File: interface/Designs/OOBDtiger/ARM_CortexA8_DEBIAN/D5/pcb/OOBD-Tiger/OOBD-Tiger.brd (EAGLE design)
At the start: 63.4 x 38.2 mm, 112 parts, among them IC1 ADM3053M, IC2 ADM3053M, IC4 DS3231, U1 SY6280, U10 MP1482DS, U2 SN65HVD230(SO8), U3 SY6280, U6 SN65HVD230(SO8)

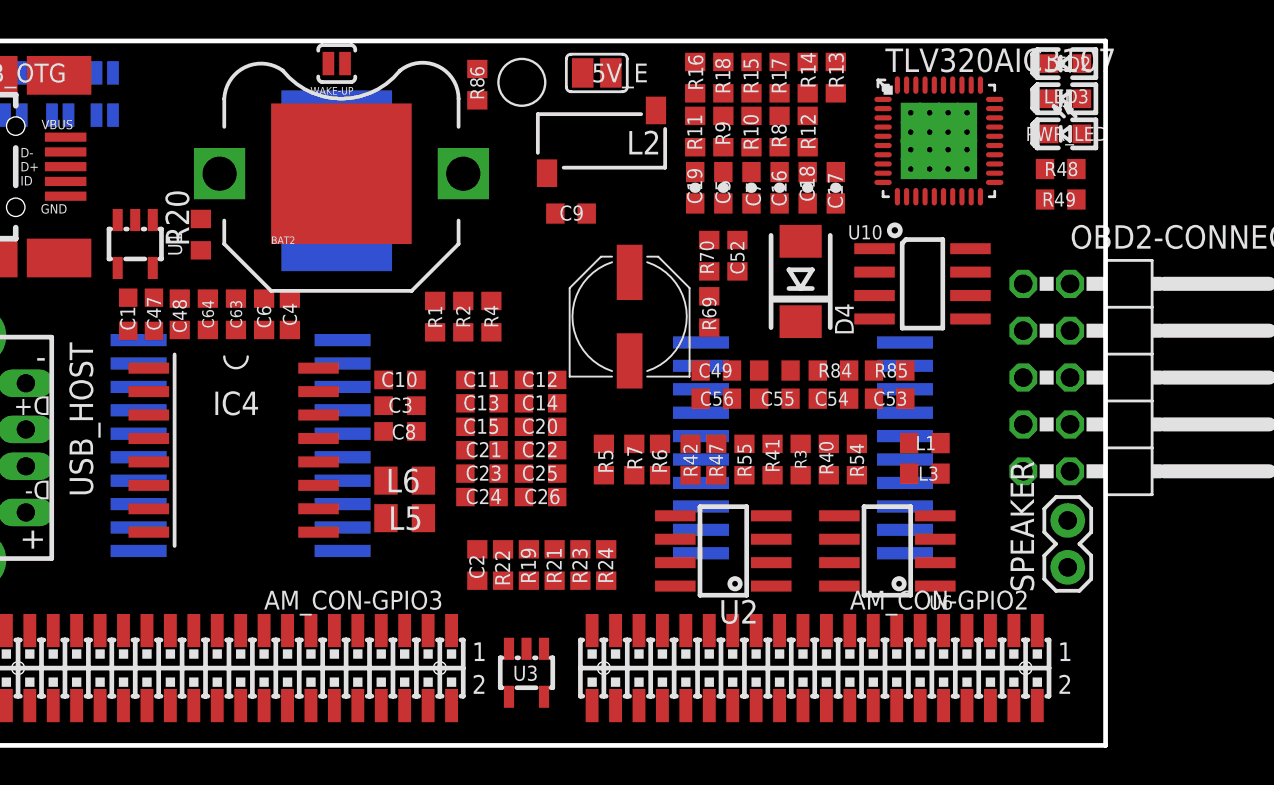
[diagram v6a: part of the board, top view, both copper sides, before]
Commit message: Erster adm3053 Plazierungsversuch, Kondensatoren nahe an IC, aber nicht so nah wie in der Alpnote.
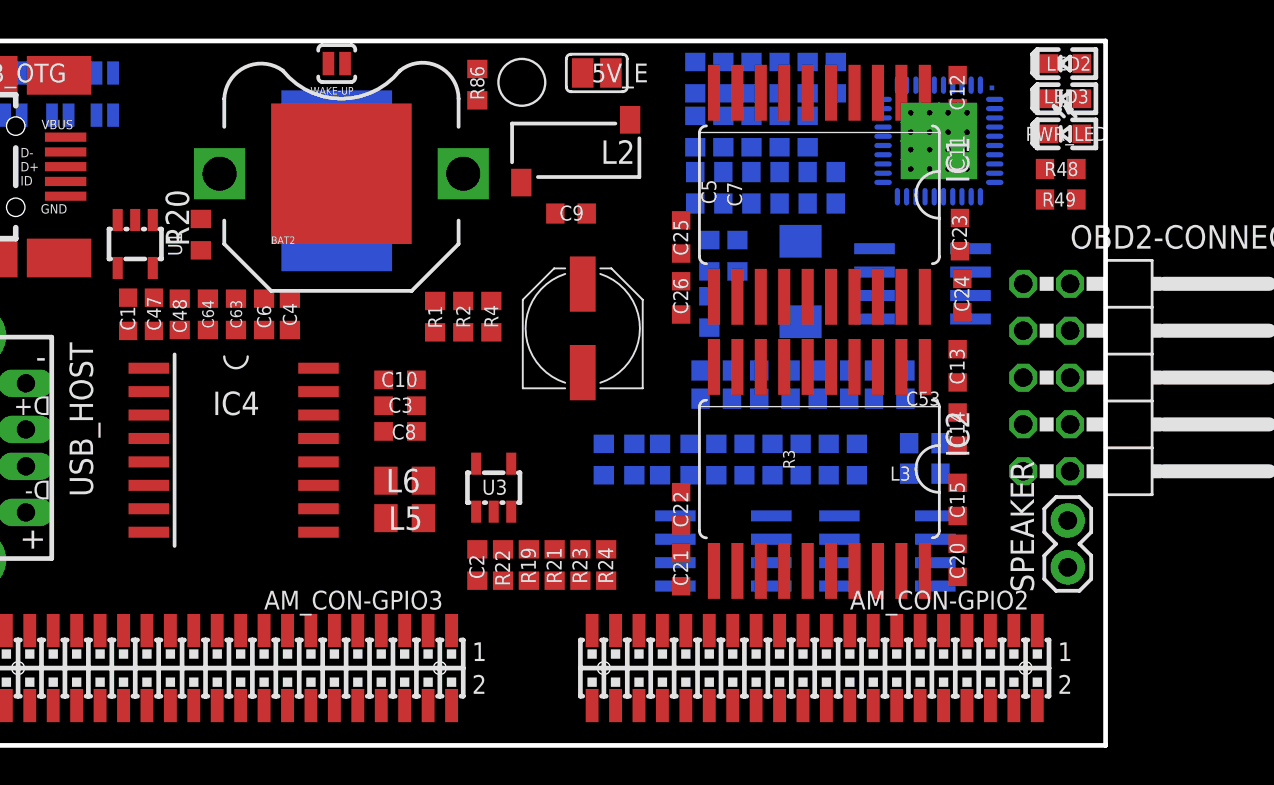
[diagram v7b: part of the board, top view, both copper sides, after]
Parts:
- moved IC1 34.2 mm to (47.9, 29.8), flipped to the top, turned to 180 degrees
- moved C23 29.0 mm to (55.5, 27.7), turned to 90 degrees
- moved C11 28.6 mm to (55.4, 32.1), turned to 90 degrees
- moved C24 28.2 mm to (55.6, 24.4), turned to 90 degrees
- moved C12 27.5 mm to (55.4, 35.4), turned to 90 degrees
- moved C15 26.1 mm to (55.4, 13.3), turned to 90 degrees
- moved C13 25.9 mm to (55.4, 20.6), turned to 90 degrees
- moved C20 23.7 mm to (55.4, 10.0), turned to 90 degrees
- moved C14 22.6 mm to (55.4, 17.1), turned to 90 degrees
- moved C25 14.9 mm to (40.4, 27.6), turned to 90 degrees
- moved C26 13.2 mm to (40.4, 24.3), turned to 90 degrees
- moved C21 12.6 mm to (40.4, 9.53), turned to 90 degrees
- moved U3 10.2 mm to (30.2, 14.0), turned to 270 degrees
- moved C22 8.26 mm to (40.4, 12.8), turned to 90 degrees
- moved C51 2.62 mm to (35.1, 22.6)
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
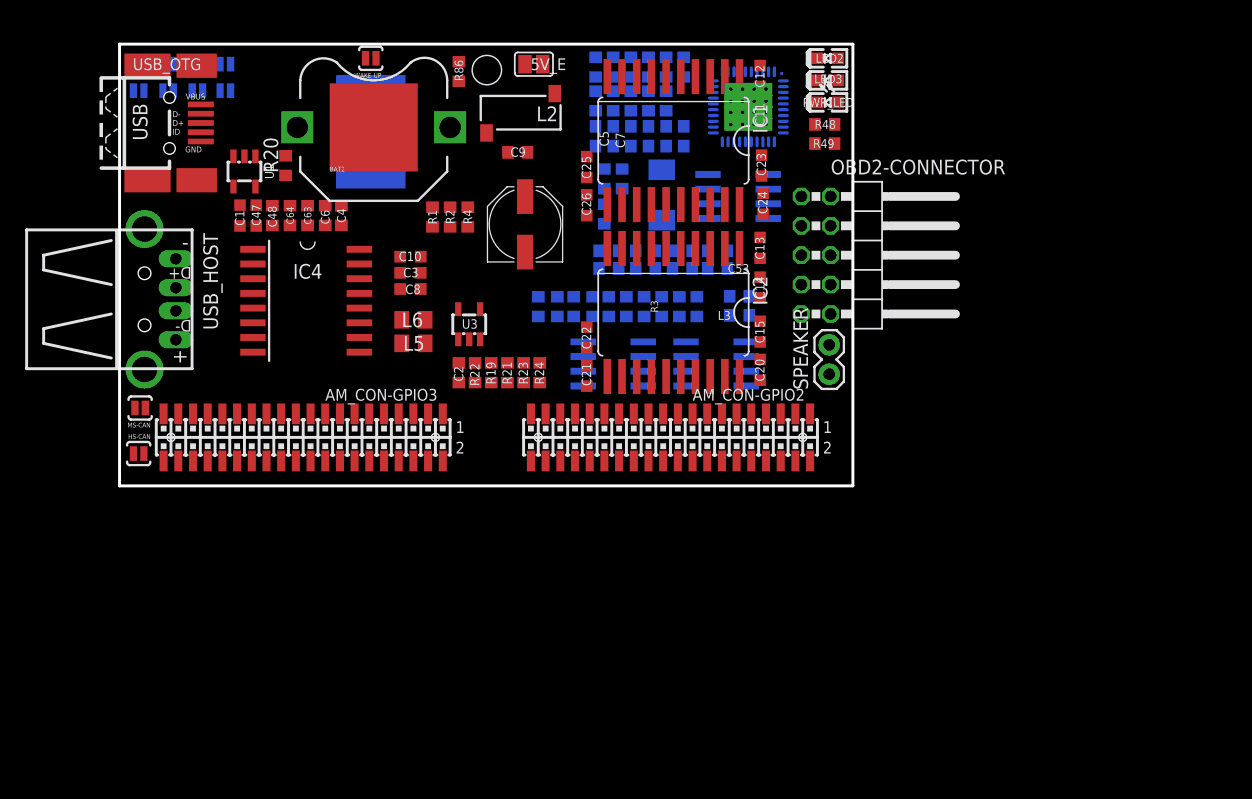
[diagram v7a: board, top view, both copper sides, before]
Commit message: fix ERC findings modify and fix ADM3053 connections remove jumper against optional 0R resistors for Standard CAN interface
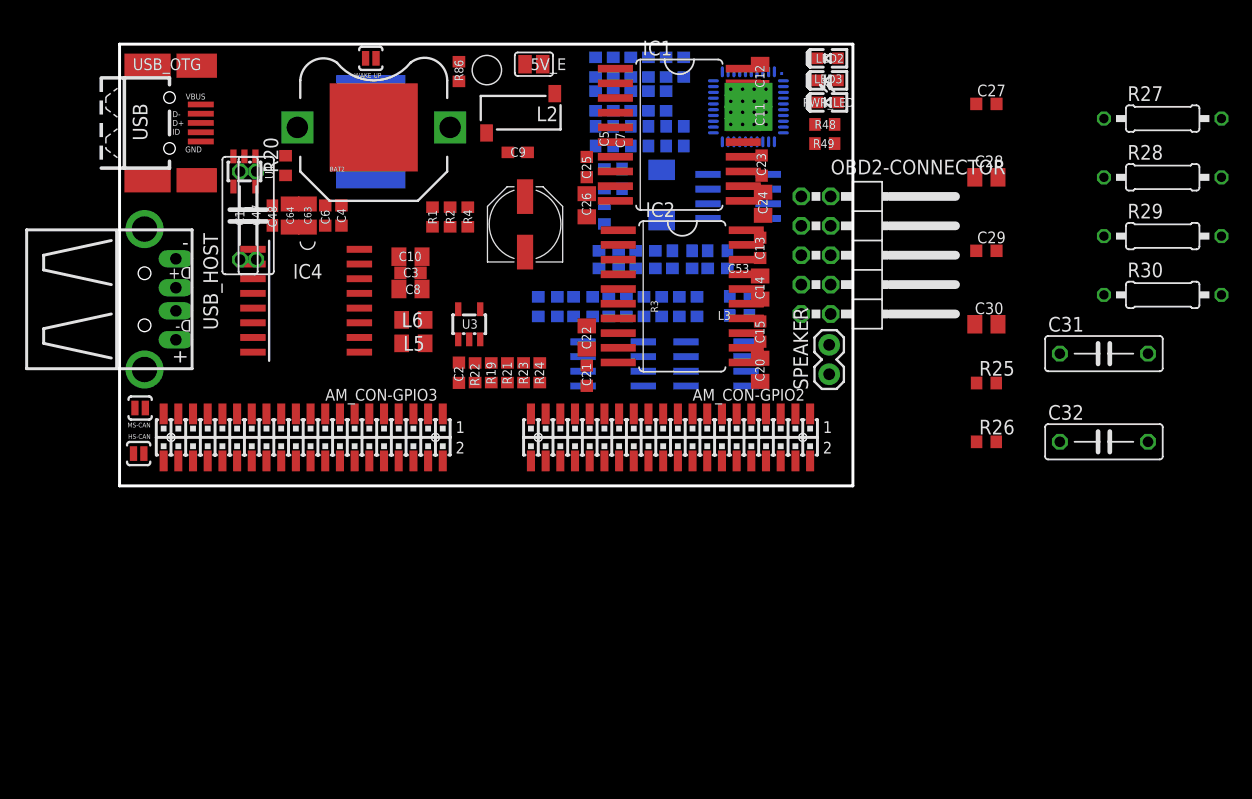
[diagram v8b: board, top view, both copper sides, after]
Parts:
- removed HS-CAN_H-DISABLE, HS-CAN_L-DISABLE, MS-CAN_H-DISABLE, MS-CAN_L-DISABLE: CLOSED, SparkFun:SJ_2S-NO
- removed HS-CAN_H-ENABLE, HS-CAN_L-ENABLE, MS-CAN_H-ENABLE, MS-CAN_L-ENABLE: OPEN (use jumper), SparkFun:SJ_2S-NO
- added C27, C29: 100nF, rcl:C0603K
- added C28, C30: 10µF, rcl:C0805K
- added C31, C32: NA (AY2221K29Y5SS63L7), rcl:C075-032X103
- added R25, R26: 8k2, rcl:R0603
- added R27, R28, R29, R30: NA (0R), rcl:0207/10
- C1, C47: device rcl:C0603_OLIMEX -> rcl:C075-032X103
- C10, C8: device rcl:C0603_DWS -> rcl:C0805K
- C11, C13, C15, C21, C23, C25: device rcl:C0603_OLIMEX -> rcl:C0603K
- C12, C14, C20, C22, C24, C26: device rcl:C0603_OLIMEX -> rcl:C0805K
- C2, C4, C6: device rcl:C0603 -> rcl:C0603K
- C3: device rcl:C0603_DWS -> rcl:C0603K
- C63, C64: device rcl:C0603 -> rcl:C0805K
- moved IC2 1.59 mm to (48.6, 16.4), turned to 270 degrees
- moved IC1 0.72 mm to (48.4, 30.4), turned to 270 degrees
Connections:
- removed net CANH: IC2.17, MS-CAN_H-ENABLE.1
- removed net CANH1: HS-CAN_H-ENABLE.2, HS-CAN_L-DISABLE.1, OBD2-CONNECTOR.7
- removed net CANL: MS-CAN.1, MS-CAN_L-DISABLE.2, U6.6
- removed net CANL1: HS-CAN.1, HS-CAN_H-DISABLE.1, U2.6
- removed net GND1: IC1.9
- removed net N$30: HS-CAN_L-DISABLE.2, R6.2, U2.7
- removed net N$32: IC2.15, MS-CAN_L-ENABLE.2
- removed net N$36: MS-CAN_L-DISABLE.1, MS-CAN_L-ENABLE.1, OBD2-CONNECTOR.2
- removed net N$37: MS-CAN_H-DISABLE.1, MS-CAN_H-ENABLE.2, OBD2-CONNECTOR.1
- removed net N$38: IC2.11, IC2.13, IC2.14, IC2.16
- removed net N$40: IC1.19
- removed net N$42: IC2.10, IC2.20, IC2.9
- removed net N$45: IC1.11, IC1.13, IC1.14, IC1.16
- removed net N$46: IC1.10, IC1.20
- removed net VCC: AM3352-SOM-EVB-PLATFORM.3-3, AM3352-SOM-EVB-PLATFORM.4-3, C1.1, C47.1, R47.2, U2.3, U6.3
- new net 3V3: AM3352-SOM-EVB-PLATFORM.3-3, AM3352-SOM-EVB-PLATFORM.4-3, C1.1, C11.1, C12.1, C13.1, C14.1, C47.1, IC1.8, IC2.8, R47.2, U2.3, U6.3
- new net CAN0_H: IC2.17, OBD2-CONNECTOR.1, R42.2, U6.7
- new net CAN0_L: IC2.15, MS-CAN.1, OBD2-CONNECTOR.2, U6.6
- new net CAN1_H: IC1.17, OBD2-CONNECTOR.7, R6.2, U2.7
- new net CAN1_L: HS-CAN.1, IC1.15, OBD2-CONNECTOR.6, U2.6
- new net GNDA: C15.2, C20.2, C21.2, C22.2, C23.2, C24.2, C25.2, C26.2, C31.1, C32.1, IC1.11, IC1.13, IC1.16, IC1.20, IC2.11, IC2.13, IC2.16, IC2.20, R25.1, R26.1
- new net N$50: C15.1, C20.1, C21.1, C22.1, IC2.12, IC2.19
- new net N$52: IC1.18, R26.2
- net +5V: now also C27.1, C28.1, C29.1, C30.1, IC2.6; no longer C11.1, C12.1, C13.1, C14.1, C15.1, C20.1, C21.1, C22.1, C23.1, C24.1, C25.1, C26.1, IC1.8, IC2.12, IC2.19, IC2.8
- net DCAN0_RX: now also R27.2
- net DCAN0_TX: now also R28.2
- net DCAN1_RX: now also R29.2
- net DCAN1_TX: now also R30.2
- net GND: now also C27.2, C28.2, C29.2, C30.2, C31.2, C32.2, IC1.10, IC1.9, IC2.10, IC2.9; no longer C15.2, C20.2, C21.2, C22.2, C23.2, C24.2, C25.2, C26.2
- net N$31: now also C23.1, C24.1, C25.1, C26.1, IC1.12, IC1.19; no longer HS-CAN_H-DISABLE.2, HS-CAN_L-ENABLE.2, OBD2-CONNECTOR.6
- net N$33: now also IC2.18, R25.2; no longer MS-CAN_H-DISABLE.2, R42.2, U6.7
- net N$34: now also IC2.4, R27.1; no longer HS-CAN_H-ENABLE.1, IC1.17
- net N$35: now also IC2.5, R28.1; no longer HS-CAN_L-ENABLE.1, IC1.15
- net N$39: now also IC1.4, R29.1; no longer IC2.6
- net N$41: now also IC1.5, R30.1; no longer IC1.12
